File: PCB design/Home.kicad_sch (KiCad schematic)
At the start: 17 parts, among them J1 Fan, J2 LCD, J3 EM LOCK, J4 ACS712 Signal, J5 Power In, J7 RFID, J8 RFID, J9 LCD, U1 ACS712, U3 DHT11, U5 PIR, U6 MQ2

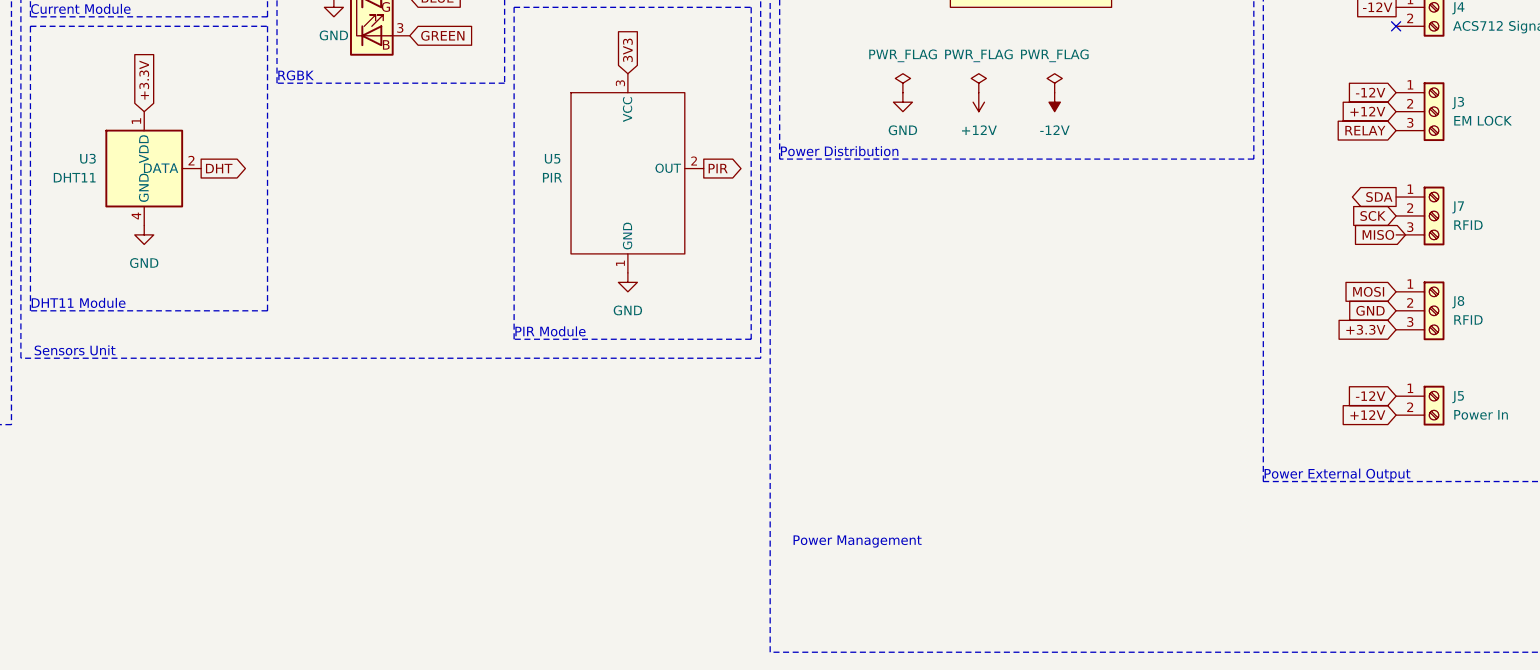
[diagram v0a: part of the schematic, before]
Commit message: added relay
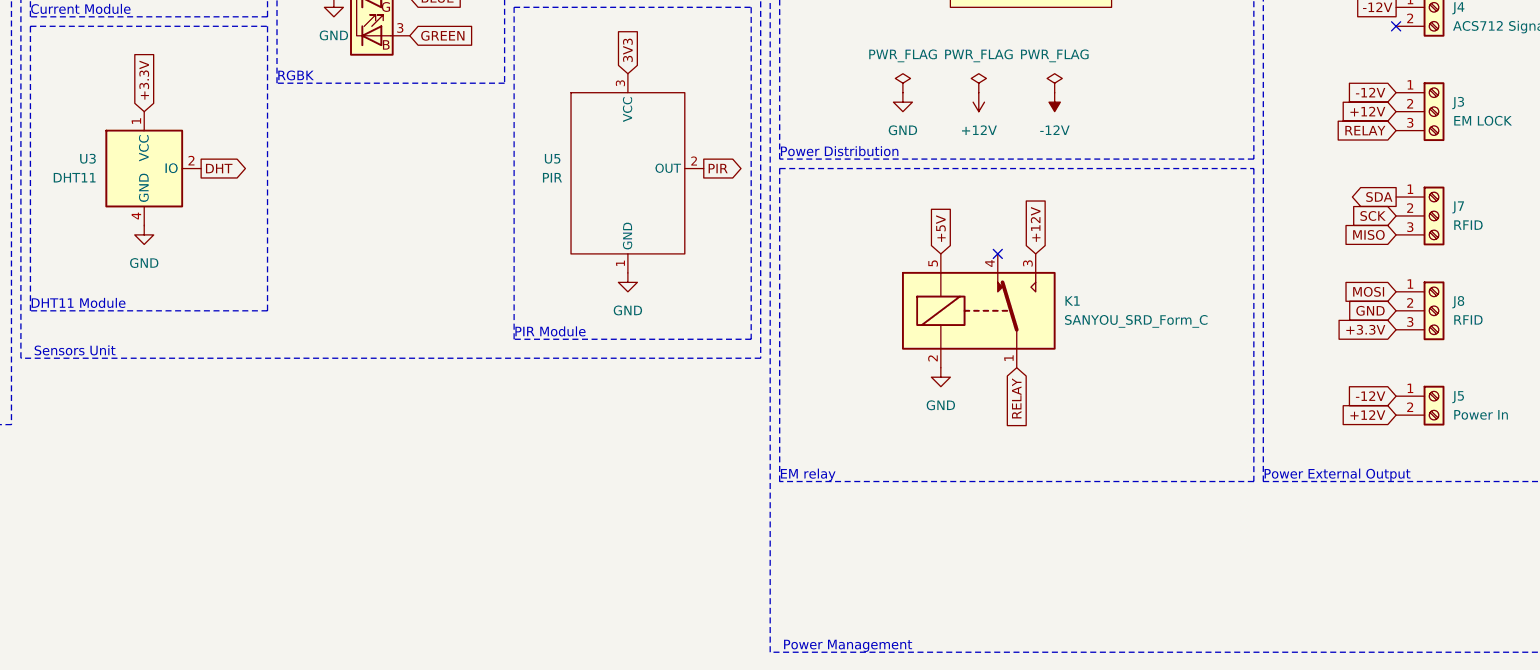
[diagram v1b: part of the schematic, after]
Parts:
- added K1: SANYOU_SRD_Form_C, Relay_THT:Relay_SPDT_SANYOU_SRD_Series_Form_C, symbol Relay:SANYOU_SRD_Form_C
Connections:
- net +12V: now also K1.3
- net +5V: now also K1.5
- net GND: now also K1.2
- net MISO: now also J7.3 (Pin_3)
- net RELAY: now also K1.1
- no-connect marks 16 -> 17
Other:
- note added: "EM relay"
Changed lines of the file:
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@@
   (no_connect (at 25.4 64.77))
   (no_connect (at 25.4 73.66))
+  (no_connect (at 204.47 87.63))
   (no_connect (at 257.81 57.15))
   (no_connect (at 25.4 71.12))
@@
     (fill (type none))
   )
+  (rectangle (start 175.26 76.2) (end 238.76 118.11)
+    (stroke (width 0) (type dash))
+    (fill (type none))
+  )
   (rectangle (start 107.95 38.1) (end 138.43 64.77)
     (stroke (width 0) (type dash))
@@
     (effects (font (size 1.27 1.27)) (justify left bottom))
   )
-  (text "Power Management" (at 194.31 127 0)
+  (text "Power Management" (at 193.04 140.97 0)
     (effects (font (size 1.27 1.27)) (justify right bottom))
   )
+  (text "EM relay" (at 175.26 118.11 0)
+    (effects (font (size 1.27 1.27)) (justify left bottom))
+  )
+  (global_label "RELAY" (shape input) (at 207.01 102.87 270) (fields_autoplaced)
+    (effects (font (size 1.27 1.27)) (justify right))
+    (property "Intersheetrefs" "${INTERSHEET_REFS}" (at 207.01 111.4001 90)
+      (effects (font (size 1.27 1.27)) (justify right) hide)
+    )
+  )
   (global_label "3V3" (shape input) (at 154.94 63.5 90) (fields_autoplaced)
     (effects (font (size 1.27 1.27)) (justify left))
@@
     )
   )
+  (global_label "+5V" (shape input) (at 196.85 87.63 90) (fields_autoplaced)
+    (effects (font (size 1.27 1.27)) (justify left))
+    (property "Intersheetrefs" "${INTERSHEET_REFS}" (at 196.85 80.8537 90)
+      (effects (font (size 1.27 1.27)) (justify left) hide)
+    )
+  )
   (global_label "+3.3V" (shape input) (at 45.72 24.13 90) (fields_autoplaced)
     (effects (font (size 1.27 1.27)) (justify left))
@@
     )
   )
-  (global_label "MISO" (shape input) (at 259.08 85.09 180) (fields_autoplaced)
-    (effects (font (size 1.27 1.27)) (justify right))
-    (property "Intersheetrefs" "${INTERSHEET_REFS}" (at 251.4986 85.09 0)
+  (global_label "MISO" (shape input) (at 257.81 85.09 180) (fields_autoplaced)
+    (effects (font (size 1.27 1.27)) (justify right))
+    (property "Intersheetrefs" "${INTERSHEET_REFS}" (at 250.2286 85.09 0)
       (effects (font (size 1.27 1.27)) (justify right) hide)
     )
@@
     (property "Intersheetrefs" "${INTERSHEET_REFS}" (at 251.2567 43.18 0)
       (effects (font (size 1.27 1.27)) (justify right) hide)
+    )
+  )
+  (global_label "+12V" (shape input) (at 209.55 87.63 90) (fields_autoplaced)
+    (effects (font (size 1.27 1.27)) (justify left))
+    (property "Intersheetrefs" "${INTERSHEET_REFS}" (at 209.55 79.6442 90)
+      (effects (font (size 1.27 1.27)) (justify left) hide)
     )
   )
@@
         (path "/118f67c1-6511-465d-942a-171badc589e3"
           (reference "#FLG03") (unit 1)
+        )
+      )
+    )
+  )
+  (symbol (lib_id "power:GND") (at 196.85 102.87 0) (unit 1)
+    (in_bom yes) (on_board yes) (dnp no) (fields_autoplaced)
+    (property "Reference" "#PWR018" (at 196.85 109.22 0)
+      (effects (font (size 1.27 1.27)) hide)
+    )
+    (property "Value" "GND" (at 196.85 107.95 0)
+      (effects (font (size 1.27 1.27)))
+    )
+    (property "Footprint" "" (at 196.85 102.87 0)
+      (effects (font (size 1.27 1.27)) hide)
+    )
+    (property "Datasheet" "" (at 196.85 102.87 0)
+      (effects (font (size 1.27 1.27)) hide)
+    )
+    (pin "1")
+    (instances
+      (project "Home"
+        (path "/118f67c1-6511-465d-942a-171badc589e3"
+          (reference "#PWR018") (unit 1)
         )
       )
@@
         )
       )
+    )
+  )
+  (symbol (lib_id "Relay:SANYOU_SRD_Form_C") (at 201.93 95.25 0) (unit 1)
+    (in_bom yes) (on_board yes) (dnp no) (fields_autoplaced)
+    (property "Reference" "K1" (at 213.36 93.98 0)
+      (effects (font (size 1.27 1.27)) (justify left))
+    )
+    (property "Value" "SANYOU_SRD_Form_C" (at 213.36 96.52 0)
+      (effects (font (size 1.27 1.27)) (justify left))
+    )
+    (property "Footprint" "Relay_THT:Relay_SPDT_SANYOU_SRD_Series_Form_C" (at 213.36 96.52 0)
+      (effects (font (size 1.27 1.27)) (justify left) hide)
+    )
+    (property "Datasheet" "http://www.sanyourelay.ca/public/products/pdf/SRD.pdf" (at 201.93 95.25 0)
+      (effects (font (size 1.27 1.27)) hide)
+    )
+    (pin "1")
+    (pin "2")
+    (pin "3")
+    (pin "4")
+    (pin "5")
+    (instances
+      (project "Home"
+        (path "/118f67c1-6511-465d-942a-171badc589e3"
+          (reference "K1") (unit 1)
+        )
+      )

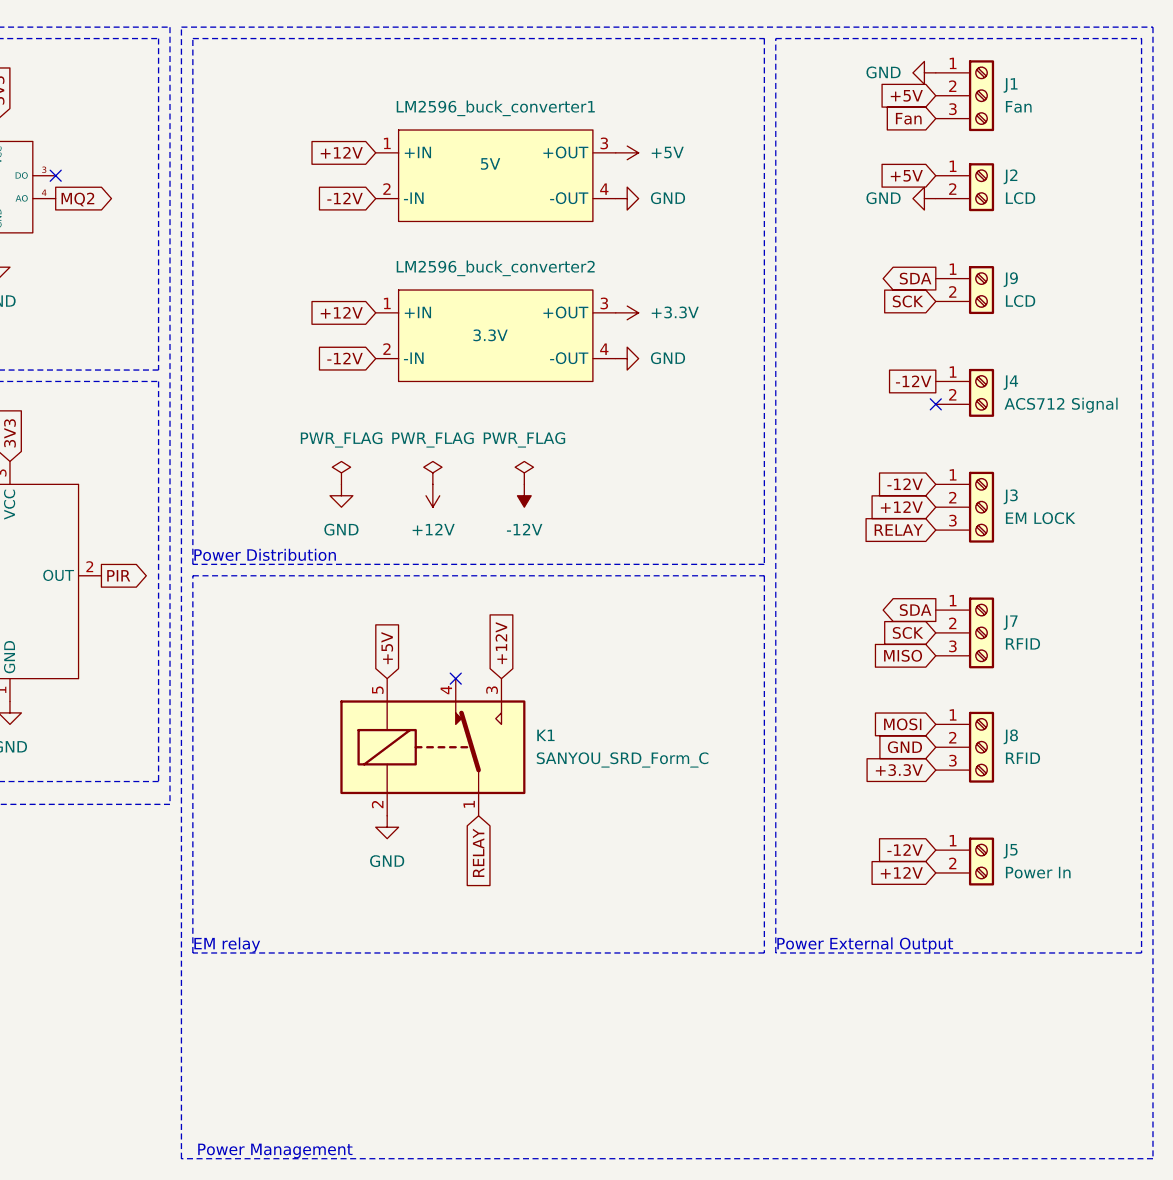
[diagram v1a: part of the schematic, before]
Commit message: edited relay
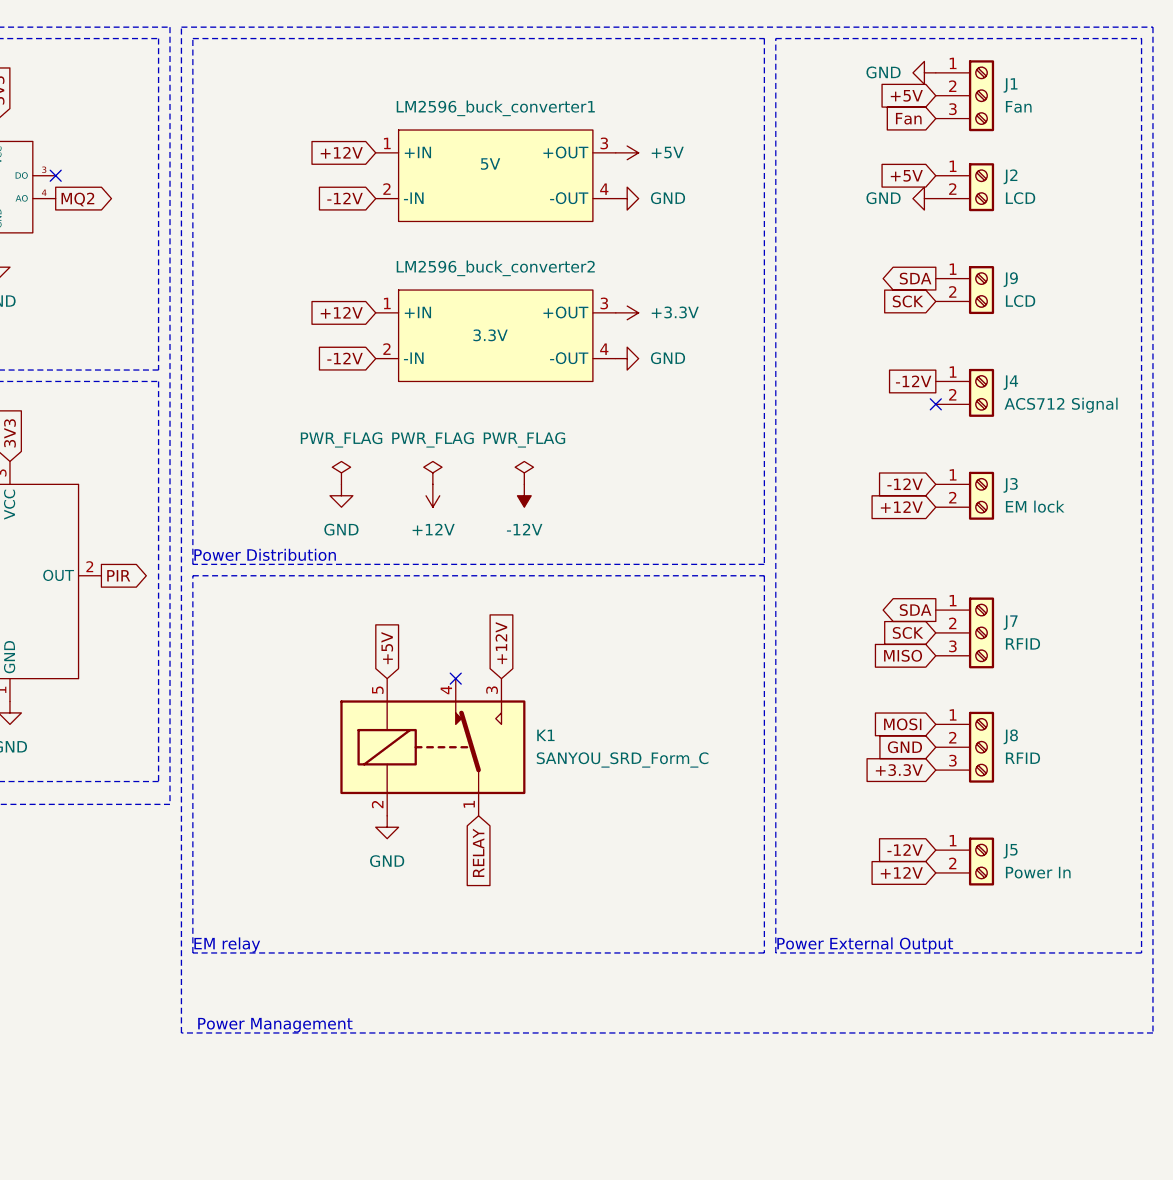
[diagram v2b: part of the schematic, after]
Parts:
- removed J3: EM LOCK, TerminalBlock:TerminalBlock_Altech_AK300-3_P5.00mm, symbol Connector:Screw_Terminal_01x03
- added J3: EM lock, TerminalBlock:TerminalBlock_Altech_AK300-2_P5.00mm, symbol Connector:Screw_Terminal_01x02
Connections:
- net +12V: now also J3.2 (Pin_2)
- net -12V: now also J3.1 (Pin_1)
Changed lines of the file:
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@@
     (fill (type none))
   )
-  (rectangle (start 173.99 15.24) (end 281.94 140.97)
+  (rectangle (start 173.99 15.24) (end 281.94 127)
     (stroke (width 0) (type dash))
     (fill (type none))
@@
     (effects (font (size 1.27 1.27)) (justify left bottom))
   )
-  (text "Power Management" (at 193.04 140.97 0)
+  (text "Power Management" (at 193.04 127 0)
     (effects (font (size 1.27 1.27)) (justify right bottom))
   )
@@
     (effects (font (size 1.27 1.27)) (justify right))
     (property "Intersheetrefs" "${INTERSHEET_REFS}" (at 18.9261 59.69 0)
-      (effects (font (size 1.27 1.27)) (justify right) hide)
-    )
-  )
-  (global_label "RELAY" (shape input) (at 257.81 71.12 180) (fields_autoplaced)
-    (effects (font (size 1.27 1.27)) (justify right))
-    (property "Intersheetrefs" "${INTERSHEET_REFS}" (at 249.2005 71.12 0)
       (effects (font (size 1.27 1.27)) (justify right) hide)
     )
@@
     )
   )
+  (symbol (lib_id "Connector:Screw_Terminal_01x02") (at 262.89 66.04 0) (unit 1)
+    (in_bom yes) (on_board yes) (dnp no) (fields_autoplaced)
+    (property "Reference" "J3" (at 265.43 66.04 0)
+      (effects (font (size 1.27 1.27)) (justify left))
+    )
+    (property "Value" "EM lock" (at 265.43 68.58 0)
+      (effects (font (size 1.27 1.27)) (justify left))
+    )
+    (property "Footprint" "TerminalBlock:TerminalBlock_Altech_AK300-2_P5.00mm" (at 262.89 66.04 0)
+      (effects (font (size 1.27 1.27)) hide)
+    )
+    (property "Datasheet" "~" (at 262.89 66.04 0)
+      (effects (font (size 1.27 1.27)) hide)
+    )
+    (pin "1")
+    (pin "2")
+    (instances
+      (project "Home"
+        (path "/118f67c1-6511-465d-942a-171badc589e3"
+          (reference "J3") (unit 1)
+        )
+      )
+    )
+  )
   (symbol (lib_id "Buck_coverter:DC-DC_LM2596_BUCK") (at 203.2 31.75 0) (unit 1)
     (in_bom yes) (on_board yes) (dnp no)
@@
         )
       )
-    )
-  )
-  (symbol (lib_id "Connector:Screw_Terminal_01x03") (at 262.89 68.58 0) (unit 1)
-    (in_bom yes) (on_board yes) (dnp no) (fields_autoplaced)
-    (property "Reference" "J3" (at 265.43 67.31 0)
-      (effects (font (size 1.27 1.27)) (justify left))
-    )
-    (property "Value" "EM LOCK" (at 265.43 69.85 0)
-      (effects (font (size 1.27 1.27)) (justify left))
-    )
-    (property "Footprint" "TerminalBlock:TerminalBlock_Altech_AK300-3_P5.00mm" (at 262.89 68.58 0)
-      (effects (font (size 1.27 1.27)) hide)
-    )
-    (property "Datasheet" "~" (at 262.89 68.58 0)
-      (effects (font (size 1.27 1.27)) hide)
-    )
-    (pin "1")
-    (pin "2")
-    (pin "3")
-    (instances
-      (project "Home"
-        (path "/118f67c1-6511-465d-942a-171badc589e3"
-          (reference "J3") (unit 1)
-        )
-      )

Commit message: corrected plots
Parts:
- added R1, R2: R, Resistor_THT:R_Axial_DIN0204_L3.6mm_D1.6mm_P5.08mm_Horizontal, symbol Device:R
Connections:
- net ACS: now also R1.2, R2.1; no longer U1.2 (OUT)
- net GND: now also R2.2
- new net: R1.1, U1.2 (OUT)
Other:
- moved on the sheet: U1, U3
